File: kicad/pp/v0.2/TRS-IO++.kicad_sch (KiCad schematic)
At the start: 98 parts, among them J1 TRS-80 M3 Pin Header, J10 AudioJack3, J11 Mini-DIN-6, J12 USB_B_Micro, J2 TRS-80 M1 Pin Connector, J3 TRS-80 M3 Edge Connector, J4 TRS-80 M1 Edge Connector, J5 Conn_01x06_Male, J6 Conn_01x06_Male, J7 HDMI_A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

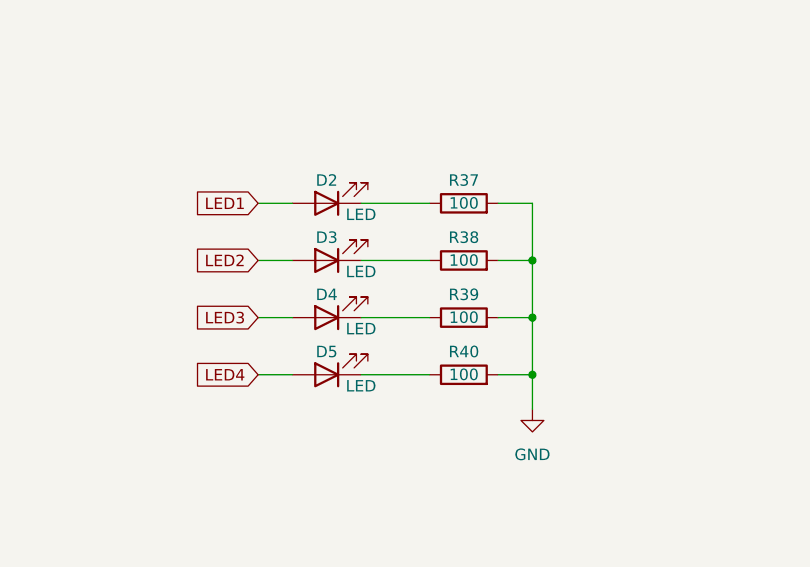
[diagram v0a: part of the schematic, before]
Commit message: Move diagnostic LEDs to PCB edge
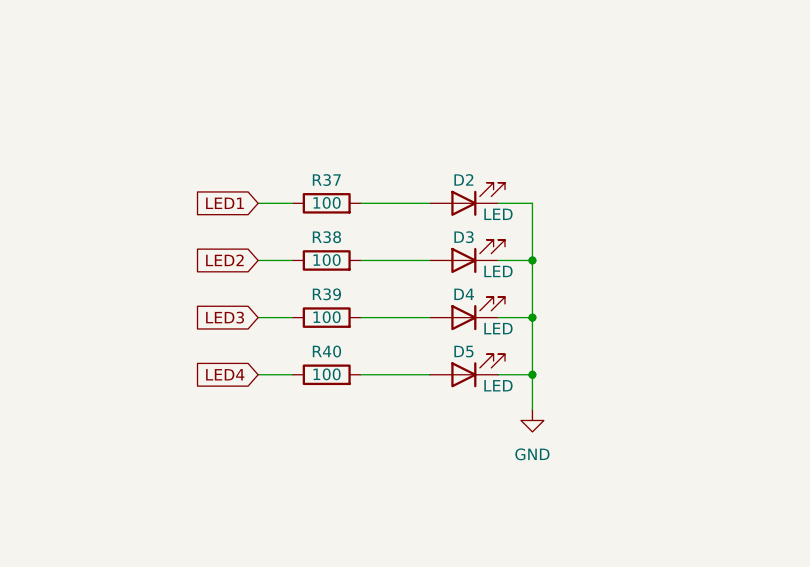
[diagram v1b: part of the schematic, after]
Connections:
- net GND: now also D2.1 (K), D3.1 (K), D4.1 (K), D5.1 (K); no longer R37.2, R38.2, R39.2, R40.2
- net LED1: now also R37.1; no longer D2.2 (A)
- net LED2: now also R38.1; no longer D3.2 (A)
- net LED3: now also R39.1; no longer D4.2 (A)
- net LED4: now also R40.1; no longer D5.2 (A)
- new net: D2.2 (A), R37.2
- new net: D4.2 (A), R39.2
- new net: D5.2 (A), R40.2
- new net: D3.2 (A), R38.2
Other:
- moved on the sheet: D2, D3, D4, D5, R37, R38, R39, R40
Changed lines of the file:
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@@
     (pin "206")
   )
-  (symbol (lib_id "Device:R") (at 176.53 204.47 90) (unit 1)
-    (in_bom yes) (on_board yes)
-    (property "Reference" "R37" (id 0) (at 176.53 201.93 90))
-    (property "Value" "100" (id 1) (at 176.53 204.47 90))
-    (property "Footprint" "Resistor_SMD:R_0805_2012Metric_Pad1.20x1.40mm_HandSolder" (id 2) (at 176.53 206.248 90)
-      (effects (font (size 1.27 1.27)) hide)
-    )
-    (property "Datasheet" "~" (id 3) (at 176.53 204.47 0)
+  (symbol (lib_id "Device:R") (at 161.29 204.47 90) (unit 1)
+    (in_bom yes) (on_board yes)
+    (property "Reference" "R37" (id 0) (at 161.29 201.93 90))
+    (property "Value" "100" (id 1) (at 161.29 204.47 90))
+    (property "Footprint" "Resistor_SMD:R_0805_2012Metric_Pad1.20x1.40mm_HandSolder" (id 2) (at 161.29 206.248 90)
+      (effects (font (size 1.27 1.27)) hide)
+    )
+    (property "Datasheet" "~" (id 3) (at 161.29 204.47 0)
       (effects (font (size 1.27 1.27)) hide)
     )
@@
     (pin "T")
   )
-  (symbol (lib_id "Device:R") (at 176.53 217.17 90) (unit 1)
-    (in_bom yes) (on_board yes)
-    (property "Reference" "R39" (id 0) (at 176.53 214.63 90))
-    (property "Value" "100" (id 1) (at 176.53 217.17 90))
-    (property "Footprint" "Resistor_SMD:R_0805_2012Metric_Pad1.20x1.40mm_HandSolder" (id 2) (at 176.53 218.948 90)
-      (effects (font (size 1.27 1.27)) hide)
-    )
-    (property "Datasheet" "~" (id 3) (at 176.53 217.17 0)
+  (symbol (lib_id "Device:R") (at 161.29 217.17 90) (unit 1)
+    (in_bom yes) (on_board yes)
+    (property "Reference" "R39" (id 0) (at 161.29 214.63 90))
+    (property "Value" "100" (id 1) (at 161.29 217.17 90))
+    (property "Footprint" "Resistor_SMD:R_0805_2012Metric_Pad1.20x1.40mm_HandSolder" (id 2) (at 161.29 218.948 90)
+      (effects (font (size 1.27 1.27)) hide)
+    )
+    (property "Datasheet" "~" (id 3) (at 161.29 217.17 0)
       (effects (font (size 1.27 1.27)) hide)
     )
@@
     (pin "2")
   )
-  (symbol (lib_id "Device:LED") (at 161.29 204.47 180) (unit 1)
-    (in_bom yes) (on_board yes)
-    (property "Reference" "D2" (id 0) (at 161.29 201.93 0))
-    (property "Value" "LED" (id 1) (at 165.1 205.74 0))
-    (property "Footprint" "LED_SMD:LED_0805_2012Metric_Pad1.15x1.40mm_HandSolder" (id 2) (at 161.29 204.47 0)
-      (effects (font (size 1.27 1.27)) hide)
-    )
-    (property "Datasheet" "~" (id 3) (at 161.29 204.47 0)
+  (symbol (lib_id "Device:LED") (at 176.53 204.47 180) (unit 1)
+    (in_bom yes) (on_board yes)
+    (property "Reference" "D2" (id 0) (at 176.53 201.93 0))
+    (property "Value" "LED" (id 1) (at 180.34 205.74 0))
+    (property "Footprint" "LED_SMD:LED_0805_2012Metric_Pad1.15x1.40mm_HandSolder" (id 2) (at 176.53 204.47 0)
+      (effects (font (size 1.27 1.27)) hide)
+    )
+    (property "Datasheet" "~" (id 3) (at 176.53 204.47 0)
       (effects (font (size 1.27 1.27)) hide)
     )
@@
     (pin "1")
   )
-  (symbol (lib_id "Device:LED") (at 161.29 217.17 180) (unit 1)
-    (in_bom yes) (on_board yes)
-    (property "Reference" "D4" (id 0) (at 161.29 214.63 0))
-    (property "Value" "LED" (id 1) (at 165.1 218.44 0))
-    (property "Footprint" "LED_SMD:LED_0805_2012Metric_Pad1.15x1.40mm_HandSolder" (id 2) (at 161.29 217.17 0)
-      (effects (font (size 1.27 1.27)) hide)
-    )
-    (property "Datasheet" "~" (id 3) (at 161.29 217.17 0)
+  (symbol (lib_id "Device:LED") (at 176.53 217.17 180) (unit 1)
+    (in_bom yes) (on_board yes)
+    (property "Reference" "D4" (id 0) (at 176.53 214.63 0))
+    (property "Value" "LED" (id 1) (at 180.34 218.44 0))
+    (property "Footprint" "LED_SMD:LED_0805_2012Metric_Pad1.15x1.40mm_HandSolder" (id 2) (at 176.53 217.17 0)
+      (effects (font (size 1.27 1.27)) hide)
+    )
+    (property "Datasheet" "~" (id 3) (at 176.53 217.17 0)
       (effects (font (size 1.27 1.27)) hide)
     )
@@
     (pin "2")
   )
-  (symbol (lib_id "Device:LED") (at 161.29 223.52 180) (unit 1)
-    (in_bom yes) (on_board yes)
-    (property "Reference" "D5" (id 0) (at 161.29 220.98 0))
-    (property "Value" "LED" (id 1) (at 165.1 224.79 0))
-    (property "Footprint" "LED_SMD:LED_0805_2012Metric_Pad1.15x1.40mm_HandSolder" (id 2) (at 161.29 223.52 0)
-      (effects (font (size 1.27 1.27)) hide)
-    )
-    (property "Datasheet" "~" (id 3) (at 161.29 223.52 0)
+  (symbol (lib_id "Device:LED") (at 176.53 223.52 180) (unit 1)
+    (in_bom yes) (on_board yes)
+    (property "Reference" "D5" (id 0) (at 176.53 220.98 0))
+    (property "Value" "LED" (id 1) (at 180.34 224.79 0))
+    (property "Footprint" "LED_SMD:LED_0805_2012Metric_Pad1.15x1.40mm_HandSolder" (id 2) (at 176.53 223.52 0)
+      (effects (font (size 1.27 1.27)) hide)
+    )
+    (property "Datasheet" "~" (id 3) (at 176.53 223.52 0)
       (effects (font (size 1.27 1.27)) hide)
     )
@@
     (pin "1")
   )
-  (symbol (lib_id "Device:LED") (at 161.29 210.82 180) (unit 1)
-    (in_bom yes) (on_board yes)
-    (property "Reference" "D3" (id 0) (at 161.29 208.28 0))
-    (property "Value" "LED" (id 1) (at 165.1 212.09 0))
-    (property "Footprint" "LED_SMD:LED_0805_2012Metric_Pad1.15x1.40mm_HandSolder" (id 2) (at 161.29 210.82 0)
-      (effects (font (size 1.27 1.27)) hide)
-    )
-    (property "Datasheet" "~" (id 3) (at 161.29 210.82 0)
+  (symbol (lib_id "Device:LED") (at 176.53 210.82 180) (unit 1)
+    (in_bom yes) (on_board yes)
+    (property "Reference" "D3" (id 0) (at 176.53 208.28 0))
+    (property "Value" "LED" (id 1) (at 180.34 212.09 0))
+    (property "Footprint" "LED_SMD:LED_0805_2012Metric_Pad1.15x1.40mm_HandSolder" (id 2) (at 176.53 210.82 0)
+      (effects (font (size 1.27 1.27)) hide)
+    )
+    (property "Datasheet" "~" (id 3) (at 176.53 210.82 0)
       (effects (font (size 1.27 1.27)) hide)
     )
@@
     (pin "2")
   )
-  (symbol (lib_id "Device:R") (at 176.53 210.82 90) (unit 1)
-    (in_bom yes) (on_board yes)
-    (property "Reference" "R38" (id 0) (at 176.53 208.28 90))
-    (property "Value" "100" (id 1) (at 176.53 210.82 90))
-    (property "Footprint" "Resistor_SMD:R_0805_2012Metric_Pad1.20x1.40mm_HandSolder" (id 2) (at 176.53 212.598 90)
-      (effects (font (size 1.27 1.27)) hide)
-    )
-    (property "Datasheet" "~" (id 3) (at 176.53 210.82 0)
+  (symbol (lib_id "Device:R") (at 161.29 210.82 90) (unit 1)
+    (in_bom yes) (on_board yes)
+    (property "Reference" "R38" (id 0) (at 161.29 208.28 90))
+    (property "Value" "100" (id 1) (at 161.29 210.82 90))
+    (property "Footprint" "Resistor_SMD:R_0805_2012Metric_Pad1.20x1.40mm_HandSolder" (id 2) (at 161.29 212.598 90)
+      (effects (font (size 1.27 1.27)) hide)
+    )
+    (property "Datasheet" "~" (id 3) (at 161.29 210.82 0)
       (effects (font (size 1.27 1.27)) hide)
     )
@@
     (pin "2")
   )
-  (symbol (lib_id "Device:R") (at 176.53 223.52 90) (unit 1)
-    (in_bom yes) (on_board yes)
-    (property "Reference" "R40" (id 0) (at 176.53 220.98 90))
-    (property "Value" "100" (id 1) (at 176.53 223.52 90))
-    (property "Footprint" "Resistor_SMD:R_0805_2012Metric_Pad1.20x1.40mm_HandSolder" (id 2) (at 176.53 225.298 90)
-      (effects (font (size 1.27 1.27)) hide)
-    )
-    (property "Datasheet" "~" (id 3) (at 176.53 223.52 0)
-      (effects (font (size 1.27 1.27)) hide)
-    )
+  (symbol (lib_id "Device:R") (at 161.29 223.52 90) (unit 1)
+    (in_bom yes) (on_board yes)
+    (property "Reference" "R40" (id 0) (at 161.29 220.98 90))
+    (property "Value" "100" (id 1) (at 161.29 223.52 90))
+    (property "Footprint" "Resistor_SMD:R_0805_2012Metric_Pad1.20x1.40mm_HandSolder" (id 2) (at 161.29 225.298 90)
+      (effects (font (size 1.27 1.27)) hide)
+    )
+    (property "Datasheet" "~" (id 3) (at 161.29 223.52 0)
+      (effects (font (size 1.27 1.27)) hide)
+    )

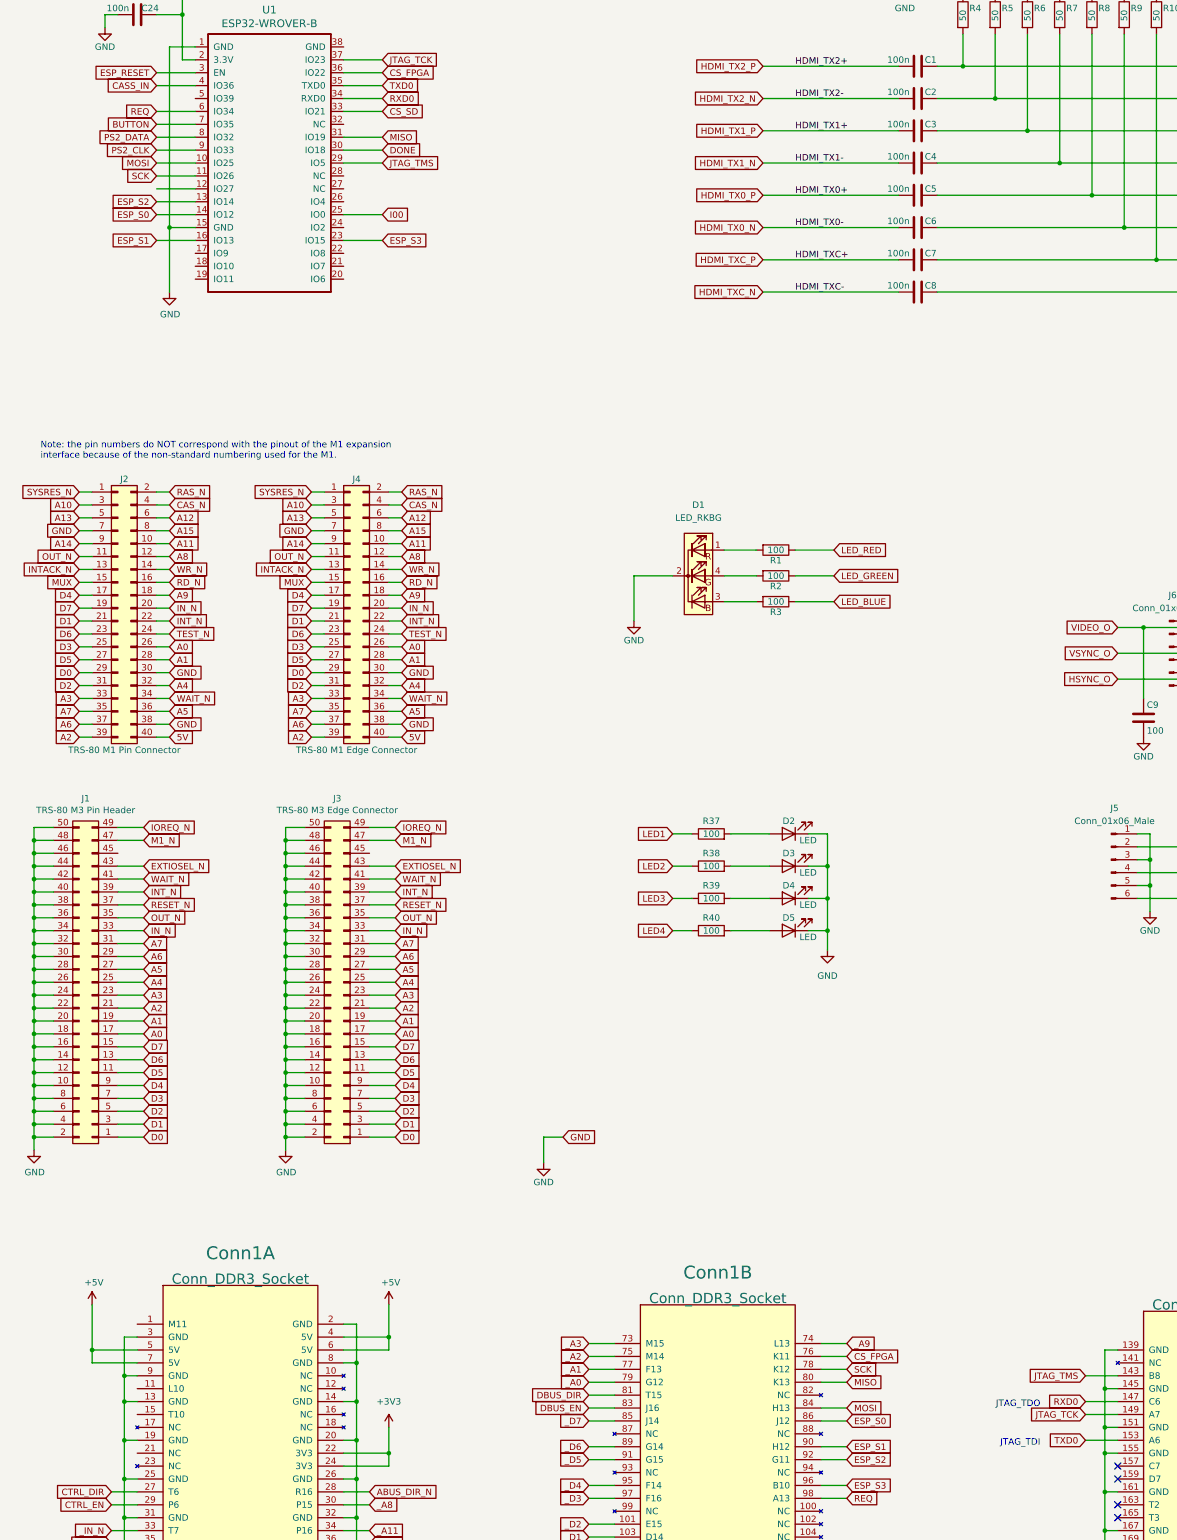
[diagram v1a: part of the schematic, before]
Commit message: Route JTAG TDI/TDO to different GPIOs
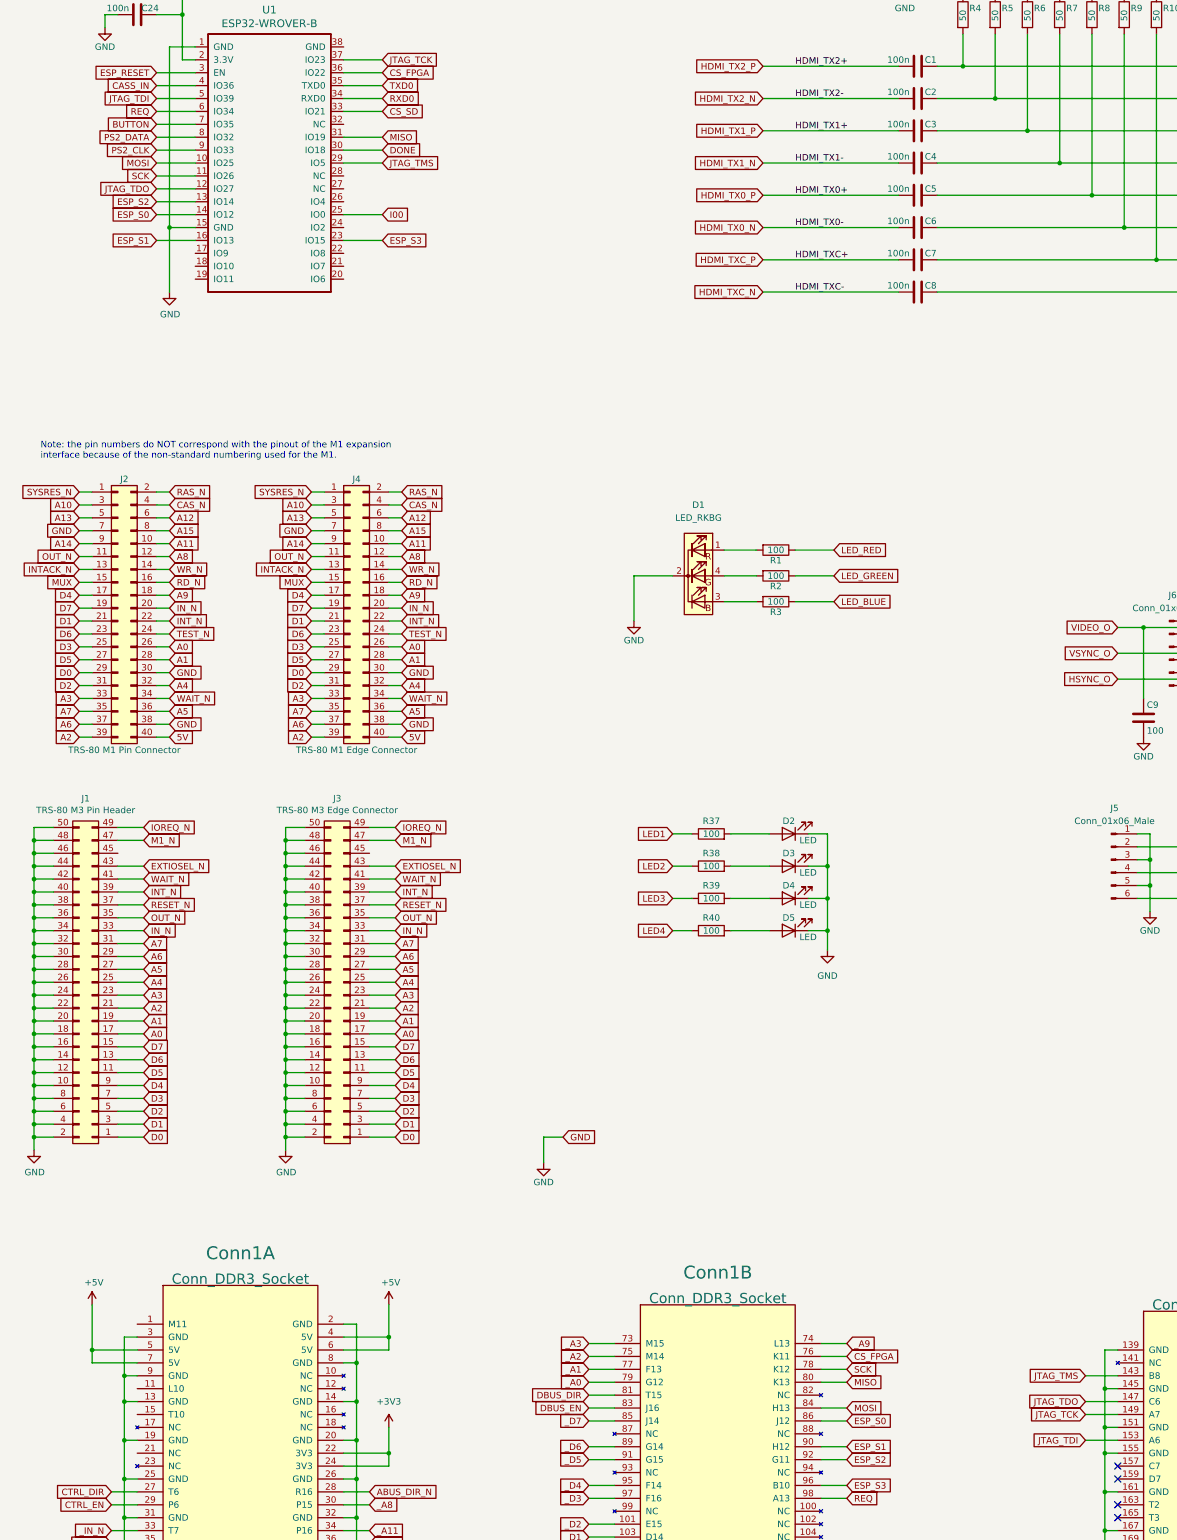
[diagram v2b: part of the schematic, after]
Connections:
- net RXD0: no longer Conn1.147 (C6)
- net TXD0: no longer Conn1.153 (A6)
- net JTAG_TDO: now reaches U1.12 (IO27)
- net JTAG_TDO: now also Conn1.147 (C6)
- net JTAG_TDI: now reaches U1.5 (IO39)
- net JTAG_TDI: now also Conn1.153 (A6)
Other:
- note removed: "JTAG_TDI"
- note removed: "JTAG_TDO"
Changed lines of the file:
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@@
     (stroke (width 0) (type default) (color 0 0 0 0))
   )
+  (wire (pts (xy 52.07 59.69) (xy 59.69 59.69))
+    (stroke (width 0) (type default) (color 0 0 0 0))
+  )
   (wire (pts (xy 281.94 321.31) (xy 288.29 321.31))
     (stroke (width 0) (type default) (color 0 0 0 0))
@@
     (stroke (width 0) (type default) (color 0 0 0 0))
   )
-  (text "JTAG_TDO" (at 226.06 317.5 180)
-    (effects (font (size 1.27 1.27)) (justify right bottom))
-  )
   (text "Note: the pin numbers do NOT correspond with the pinout of the M1 expansion\ninterface because of the non-standard numbering used for the M1."
     (at 29.21 130.81 0)
     (effects (font (size 1.27 1.27)) (justify left bottom))
   )
-  (text "JTAG_TDI" (at 226.06 325.12 180)
-    (effects (font (size 1.27 1.27)) (justify right bottom))
-  )
   (label "HDMI_TX2+" (at 177.8 53.34 0)
     (effects (font (size 1.27 1.27)) (justify left bottom))
@@
     )
   )
-  (global_label "TXD0" (shape input) (at 234.95 323.85 180) (fields_autoplaced)
+  (global_label "JTAG_TDI" (shape input) (at 234.95 323.85 180) (fields_autoplaced)
     (effects (font (size 1.27 1.27)) (justify right))
-    (property "Intersheet References" "${INTERSHEET_REFS}" (id 0) (at 336.55 359.41 0)
-      (effects (font (size 1.27 1.27)) hide)
+    (property "Intersheet References" "${INTERSHEET_REFS}" (id 0) (at 224.4331 323.7706 0)
+      (effects (font (size 1.27 1.27)) (justify right) hide)
     )
   )
@@
     )
   )
-  (global_label "RXD0" (shape input) (at 234.95 316.23 180) (fields_autoplaced)
+  (global_label "JTAG_TDO" (shape input) (at 234.95 316.23 180) (fields_autoplaced)
     (effects (font (size 1.27 1.27)) (justify right))
-    (property "Intersheet References" "${INTERSHEET_REFS}" (id 0) (at 322.58 354.33 0)
-      (effects (font (size 1.27 1.27)) hide)
+    (property "Intersheet References" "${INTERSHEET_REFS}" (id 0) (at 223.7074 316.1506 0)
+      (effects (font (size 1.27 1.27)) (justify right) hide)
     )
   )
@@
     )
   )
+  (global_label "JTAG_TDI" (shape input) (at 52.07 59.69 180) (fields_autoplaced)
+    (effects (font (size 1.27 1.27)) (justify right))
+    (property "Intersheet References" "${INTERSHEET_REFS}" (id 0) (at 41.5531 59.6106 0)
+      (effects (font (size 1.27 1.27)) (justify right) hide)
+    )
+  )
   (global_label "D6" (shape input) (at 82.55 165.1 180) (fields_autoplaced)
     (effects (font (size 1.27 1.27)) (justify right))
@@
     )
   )
+  (global_label "JTAG_TDO" (shape input) (at 52.07 77.47 180) (fields_autoplaced)
+    (effects (font (size 1.27 1.27)) (justify right))
+    (property "Intersheet References" "${INTERSHEET_REFS}" (id 0) (at 40.8274 77.3906 0)
+      (effects (font (size 1.27 1.27)) (justify right) hide)
+    )
+  )
